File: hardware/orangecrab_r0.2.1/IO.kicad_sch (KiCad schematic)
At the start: 37 parts, among them J3 USB_C_Receptacle_USB2.0, SW1 SW_Push, U9 74HC4067BQ

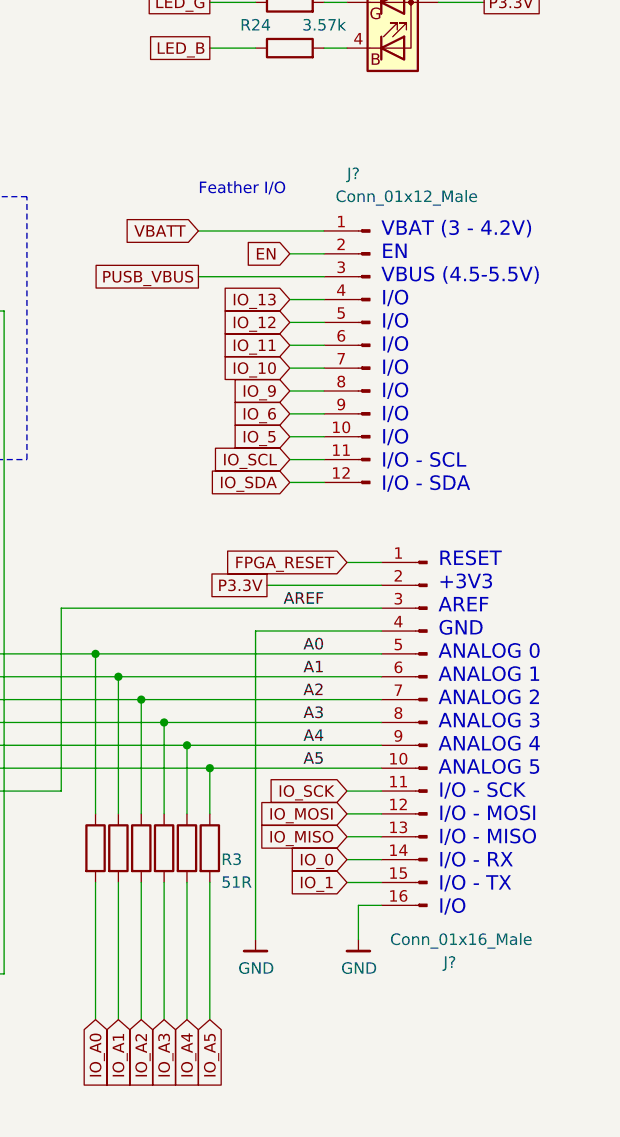
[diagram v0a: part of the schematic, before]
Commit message: hw.r0p2p1: Copy/Paste FPGA sheet contents
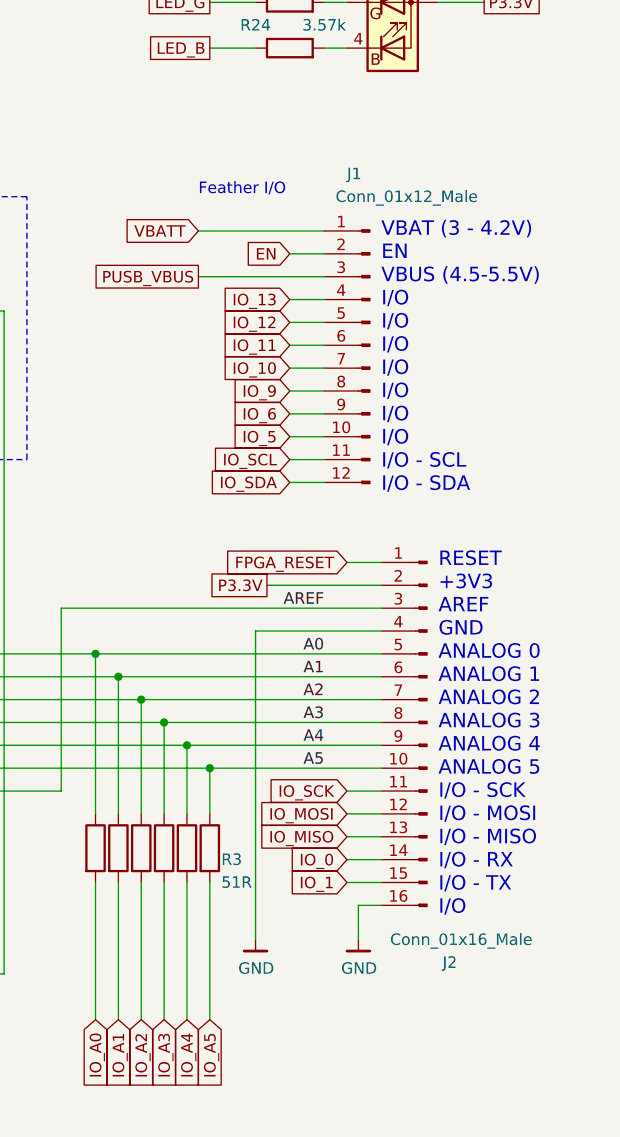
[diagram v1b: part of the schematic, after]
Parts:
- gave numbers to parts that had none: 2
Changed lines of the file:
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@@
 	(label "A3"
 		(at 218.44 114.3 180)
+		(fields_autoplaced yes)
 		(effects
 			(font
@@
 	(label "_USB_D_P"
 		(at 63.5 64.77 0)
+		(fields_autoplaced yes)
 		(effects
 			(font
@@
 	(label "A0"
 		(at 218.44 106.68 180)
+		(fields_autoplaced yes)
 		(effects
 			(font
@@
 	(label "A2"
 		(at 218.44 111.76 180)
+		(fields_autoplaced yes)
 		(effects
 			(font
@@
 	(label "A4"
 		(at 218.44 116.84 180)
+		(fields_autoplaced yes)
 		(effects
 			(font
@@
 	(label "AREF"
 		(at 218.44 101.6 180)
+		(fields_autoplaced yes)
 		(effects
 			(font
@@
 	(label "A1"
 		(at 218.44 109.22 180)
+		(fields_autoplaced yes)
 		(effects
 			(font
@@
 	(label "A5"
 		(at 218.44 119.38 180)
+		(fields_autoplaced yes)
 		(effects
 			(font
@@
 	(label "_USB_D_N"
 		(at 63.5 67.31 0)
+		(fields_autoplaced yes)
 		(effects
 			(font
@@
 	(label "_USB_D_P"
 		(at 33.02 140.97 0)
+		(fields_autoplaced yes)
 		(effects
 			(font
@@
 	(label "_USB_D_N"
 		(at 33.02 143.51 0)
+		(fields_autoplaced yes)
 		(effects
 			(font
@@
 		(on_board yes)
 		(dnp no)
-		(property "Reference" "J?"
+		(property "Reference" "J2"
 			(at 232.41 140.97 0)
 			(effects
@@
 		(instances
 			(project "OrangeCrab"
-				(path "/e2139f5f-1e2a-4e6a-b8f5-bf5d629175a9/00000000-0000-0000-0000-00005d1738db"
-					(reference "J?")
-					(unit 1)
-				)
 				(path "/e2139f5f-1e2a-4e6a-b8f5-bf5d629175a9/00000000-0000-0000-0000-00005abc9a87"
 					(reference "J2")
@@
 		(on_board yes)
 		(dnp no)
-		(property "Reference" "J?"
+		(property "Reference" "J1"
 			(at 220.98 53.34 0)
 			(effects
@@
 		(instances
 			(project "OrangeCrab"
-				(path "/e2139f5f-1e2a-4e6a-b8f5-bf5d629175a9/00000000-0000-0000-0000-00005d1738db"
-					(reference "J?")
-					(unit 1)
-				)
 				(path "/e2139f5f-1e2a-4e6a-b8f5-bf5d629175a9/00000000-0000-0000-0000-00005abc9a87"
 					(reference "J1")
@@
 					(unit 1)
 				)
-				(path "/e2139f5f-1e2a-4e6a-b8f5-bf5d629175a9/00000000-0000-0000-0000-00005d1738db"
-					(reference "#PWR?")
-					(unit 1)
-				)
 			)
 		)
@@
 					(unit 1)
 				)
-				(path "/e2139f5f-1e2a-4e6a-b8f5-bf5d629175a9/00000000-0000-0000-0000-00005d1738db"
-					(reference "#PWR?")
-					(unit 1)
-				)
